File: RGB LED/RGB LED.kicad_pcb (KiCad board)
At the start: 2 copper layers, 80 x 75 mm, 81 parts, among them J1 USB_C_Receptacle_USB2.0_16P, SW1 SW_SPST, SW2 SW_SPST, U1 AP2112K-3.3, U2 MAX7219, U3 ESP32-S3-WROOM-1-N4

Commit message: schematic edits
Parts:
- added R4: 10K, Resistor_SMD:R_0603_1608Metric, F.Cu at (121.0, 82.9)
- C4: value 1uf 6.3V Y5V -> 1uF 6.3V Y5V
- D1, D2, D3, D4, D5, D6, D7, D8: value LED -> Green LED
- D10, D11, D12, D13, D14, D15, D16, D9: value LED -> Dark Blue LED
- D17, D19, D21, D23, D25, D27, D29, D31: value LED -> White LED
- D18, D20, D22, D24, D26, D28, D30, D32: value LED -> Purple LED
- D33, D37, D41, D45, D49, D53, D57, D61: value LED -> Red LED
- D34, D38, D42, D46, D50, D54, D58, D62: value LED -> Orange LED
- D35, D39, D43, D47, D51, D55, D59, D63: value LED -> Yellow LED
- D36, D40, D44, D48, D52, D56, D60, D64: value LED -> Light Blue LED
- R1: value 10k -> 5.1K 1%
- SW1, SW2: value SW_SPST -> SW_SPST_FSMSM
- TP1: value TestPoint -> RCWTE
- renumbered CIN1 to C5, COUT1 to C6
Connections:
- D65 pad 1: /ESP32/NEOPIXEL_PWR -> unconnected-(D65-DOUT-Pad1)
- D65 pad 3: unconnected-(D65-DIN-Pad3) -> /ESP32/NEOPIXEL
- D65 pad 4: /ESP32/NEOPIXEL -> /ESP32/NEOPIXEL_PWR
- U2 pad 18: unconnected-(U2-ISET-Pad18) -> Net-(U2-ISET)

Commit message: layout update
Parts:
- moved C6 70.3 mm to (75.8, 22.9)
- moved C5 70.3 mm to (75.8, 20.4)
- moved U1 70.3 mm to (80.4, 21.4)
- moved D14 59.2 mm to (96.3, 95.6)
- moved D15 59.2 mm to (96.3, 98.2)
- moved D19 59.2 mm to (96.3, 108.5)
- moved D20 59.2 mm to (96.3, 111.1)
- moved D25 59.2 mm to (100.4, 95.6)
- moved D26 59.2 mm to (100.4, 98.2)
- moved D3 59.2 mm to (92.3, 95.6)
- moved D30 59.2 mm to (100.4, 108.5)
- moved D36 59.2 mm to (104.4, 95.6)
- moved D37 59.2 mm to (104.4, 98.2)
- moved D4 59.2 mm to (92.3, 98.2)
- moved D41 59.2 mm to (104.4, 108.5)
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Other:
- board size 80 x 75 mm -> 119.2 x 110.4 mm

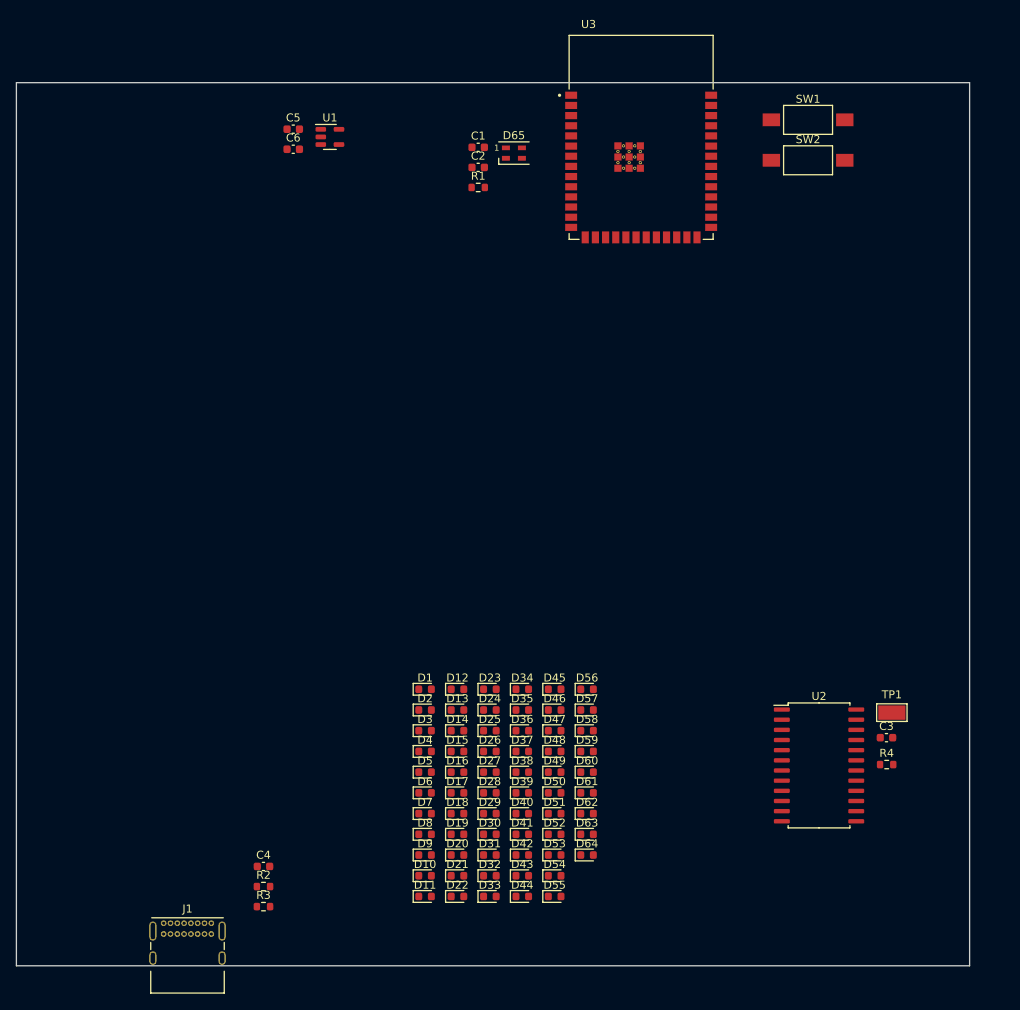
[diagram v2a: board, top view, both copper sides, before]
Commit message: changed layout, added traces/vias
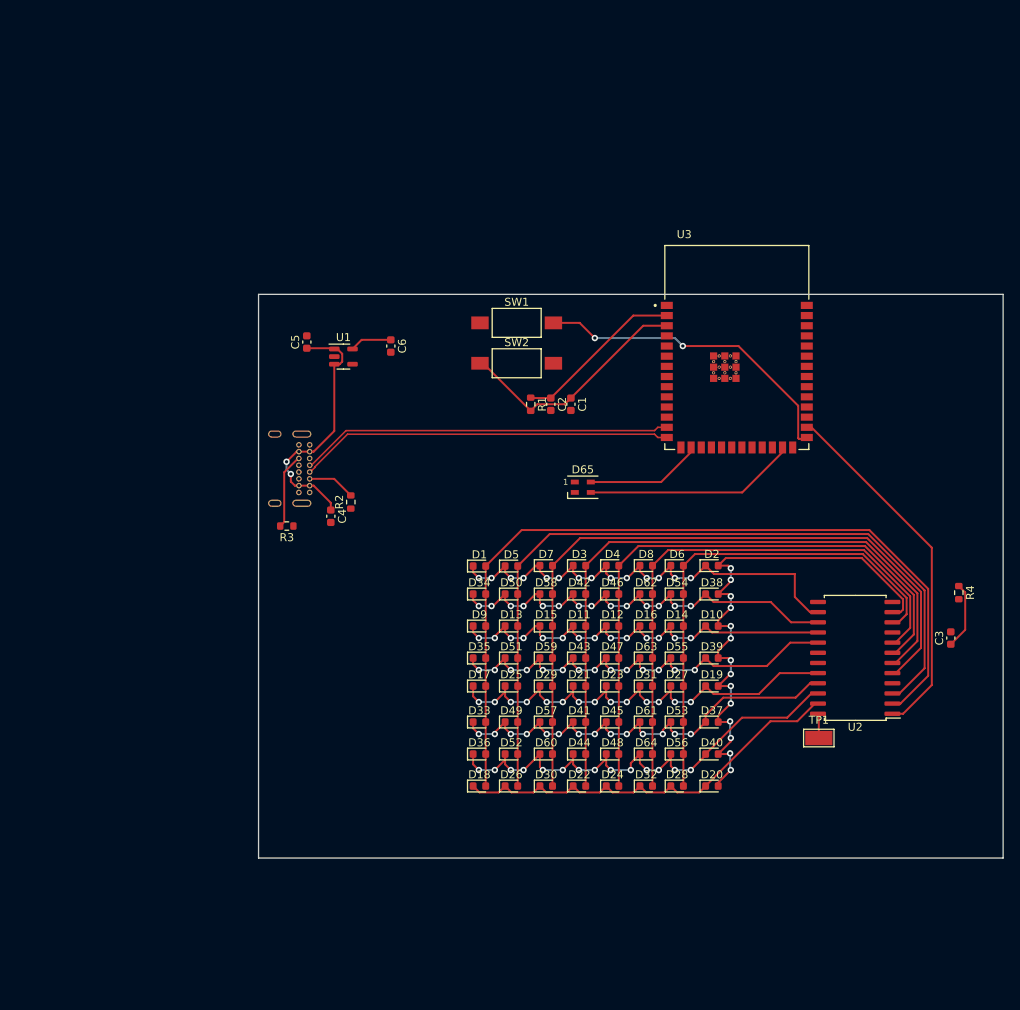
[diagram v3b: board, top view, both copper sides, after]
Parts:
- J1: moved to B.Cu
- moved J1 56.9 mm to (77.9, 65.8), turned to 90 degrees
- moved R2 49.3 mm to (83.0, 67.0), turned to 90 degrees
- moved R3 47.7 mm to (75.0, 70.0), turned to 180 degrees
- moved D10 47.5 mm to (128.1, 82.5)
- moved C4 44.6 mm to (80.5, 68.8), turned to -90 degrees
- moved SW1 44.4 mm to (103.7, 44.6)
- moved SW2 44.4 mm to (103.7, 49.7)
- moved D8 43.5 mm to (119.9, 75.0)
- moved D65 42.7 mm to (112.0, 65.2)
- moved D6 42.4 mm to (123.8, 75.0)
- moved D2 40.1 mm to (128.1, 75.0)
- moved D11 38.9 mm to (111.6, 82.5)
- moved D54 38.4 mm to (123.8, 78.5)
- moved D19 36.8 mm to (128.1, 90.0)
- moved D7 34.5 mm to (107.4, 75.0)
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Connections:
- D10 pad 2: /LED_Matrix/DIG_0 -> /LED_Matrix/DIG_1
- D11 pad 2: /LED_Matrix/DIG_0 -> /LED_Matrix/DIG_2
- D12 pad 2: /LED_Matrix/DIG_0 -> /LED_Matrix/DIG_3
- D13 pad 2: /LED_Matrix/DIG_0 -> /LED_Matrix/DIG_4
- D14 pad 2: /LED_Matrix/DIG_0 -> /LED_Matrix/DIG_5
- D15 pad 2: /LED_Matrix/DIG_0 -> /LED_Matrix/DIG_6
- D19 pad 2: /LED_Matrix/DIG_0 -> /LED_Matrix/DIG_1
- D2 pad 2: /LED_Matrix/DIG_0 -> /LED_Matrix/DIG_1
- D20 pad 2: /LED_Matrix/DIG_0 -> /LED_Matrix/DIG_1
- D21 pad 2: /LED_Matrix/DIG_0 -> /LED_Matrix/DIG_2
- D22 pad 2: /LED_Matrix/DIG_0 -> /LED_Matrix/DIG_2
- D23 pad 2: /LED_Matrix/DIG_0 -> /LED_Matrix/DIG_3
- D24 pad 2: /LED_Matrix/DIG_0 -> /LED_Matrix/DIG_3
- D25 pad 2: /LED_Matrix/DIG_0 -> /LED_Matrix/DIG_4
- D26 pad 2: /LED_Matrix/DIG_0 -> /LED_Matrix/DIG_4
- D27 pad 2: /LED_Matrix/DIG_0 -> /LED_Matrix/DIG_5
- D28 pad 2: /LED_Matrix/DIG_0 -> /LED_Matrix/DIG_5
- D29 pad 2: /LED_Matrix/DIG_0 -> /LED_Matrix/DIG_6
- D3 pad 2: /LED_Matrix/DIG_0 -> /LED_Matrix/DIG_2
- D30 pad 2: /LED_Matrix/DIG_0 -> /LED_Matrix/DIG_6
- D36 pad 1: /LED_Matrix/DIG_0 -> /LED_Matrix/SEG_DP
- D37 pad 2: /LED_Matrix/DIG_0 -> /LED_Matrix/DIG_1
- D38 pad 2: /LED_Matrix/DIG_0 -> /LED_Matrix/DIG_1
- D39 pad 2: /LED_Matrix/DIG_0 -> /LED_Matrix/DIG_1
- D4 pad 2: /LED_Matrix/DIG_0 -> /LED_Matrix/DIG_3
- D40 pad 1: /LED_Matrix/DIG_0 -> /LED_Matrix/SEG_DP
- D40 pad 2: /LED_Matrix/DIG_0 -> /LED_Matrix/DIG_1
- D41 pad 2: /LED_Matrix/DIG_0 -> /LED_Matrix/DIG_2
- D42 pad 2: /LED_Matrix/DIG_0 -> /LED_Matrix/DIG_2
- D43 pad 2: /LED_Matrix/DIG_0 -> /LED_Matrix/DIG_2
- D44 pad 1: /LED_Matrix/DIG_0 -> /LED_Matrix/SEG_DP
- D44 pad 2: /LED_Matrix/DIG_0 -> /LED_Matrix/DIG_2
- D45 pad 2: /LED_Matrix/DIG_0 -> /LED_Matrix/DIG_3
- D46 pad 2: /LED_Matrix/DIG_0 -> /LED_Matrix/DIG_3
- D47 pad 2: /LED_Matrix/DIG_0 -> /LED_Matrix/DIG_3
- D48 pad 1: /LED_Matrix/DIG_0 -> /LED_Matrix/SEG_DP
- D48 pad 2: /LED_Matrix/DIG_0 -> /LED_Matrix/DIG_3
- D49 pad 2: /LED_Matrix/DIG_0 -> /LED_Matrix/DIG_4
- D5 pad 2: /LED_Matrix/DIG_0 -> /LED_Matrix/DIG_4
- D50 pad 2: /LED_Matrix/DIG_0 -> /LED_Matrix/DIG_4
- D51 pad 2: /LED_Matrix/DIG_0 -> /LED_Matrix/DIG_4
- D52 pad 1: /LED_Matrix/DIG_0 -> /LED_Matrix/SEG_DP
- D52 pad 2: /LED_Matrix/DIG_0 -> /LED_Matrix/DIG_4
- D53 pad 2: /LED_Matrix/DIG_0 -> /LED_Matrix/DIG_5
- D54 pad 2: /LED_Matrix/DIG_0 -> /LED_Matrix/DIG_5
- D55 pad 2: /LED_Matrix/DIG_0 -> /LED_Matrix/DIG_5
- D56 pad 1: /LED_Matrix/DIG_0 -> /LED_Matrix/SEG_DP
- D56 pad 2: /LED_Matrix/DIG_0 -> /LED_Matrix/DIG_5
- D57 pad 2: /LED_Matrix/DIG_0 -> /LED_Matrix/DIG_6
- D58 pad 2: /LED_Matrix/DIG_0 -> /LED_Matrix/DIG_6
- D59 pad 2: /LED_Matrix/DIG_0 -> /LED_Matrix/DIG_6
- D6 pad 2: /LED_Matrix/DIG_0 -> /LED_Matrix/DIG_5
- D60 pad 1: /LED_Matrix/DIG_0 -> /LED_Matrix/SEG_DP
- D60 pad 2: /LED_Matrix/DIG_0 -> /LED_Matrix/DIG_6
- D64 pad 1: /LED_Matrix/DIG_0 -> /LED_Matrix/SEG_DP
- D7 pad 2: /LED_Matrix/DIG_0 -> /LED_Matrix/DIG_6
- U2 pad 10: /LED_Matrix/DIG_0 -> /LED_Matrix/DIG_5
- U2 pad 11: /LED_Matrix/DIG_0 -> /LED_Matrix/DIG_1
- U2 pad 22: /LED_Matrix/DIG_0 -> /LED_Matrix/SEG_DP
- U2 pad 3: /LED_Matrix/DIG_0 -> /LED_Matrix/DIG_4
- U2 pad 5: /LED_Matrix/DIG_0 -> /LED_Matrix/DIG_6
- U2 pad 6: /LED_Matrix/DIG_0 -> /LED_Matrix/DIG_2
- U2 pad 7: /LED_Matrix/DIG_0 -> /LED_Matrix/DIG_3
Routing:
- net /LED_Matrix/DIG_0: track 0.00 -> 104.5 mm
- net /LED_Matrix/DIG_4: track 0.00 -> 98.0 mm
- net /LED_Matrix/DIG_6: track 0.00 -> 89.7 mm
- net /LED_Matrix/DIG_2: track 0.00 -> 83.1 mm
- net /LED_Matrix/DIG_3: track 0.00 -> 76.5 mm
- net /LED_Matrix/DIG_1: track 0.00 -> 71.2 mm, vias 0 -> 14
- net /LED_Matrix/DIG_7: track 0.00 -> 69.9 mm
- net /LED_Matrix/SEG_DP: track 0.00 -> 65.5 mm, vias 0 -> 14
- net /LED_Matrix/SEG_C: track 0.00 -> 63.5 mm, vias 0 -> 14
- net /LED_Matrix/DIG_5: track 0.00 -> 62.6 mm
- net /LED_Matrix/SEG_A: track 0.00 -> 59.6 mm, vias 0 -> 14
- net /LED_Matrix/SEG_E: track 0.00 -> 58.3 mm, vias 0 -> 14
- net /LED_Matrix/SEG_G: track 0.00 -> 57.7 mm, vias 0 -> 14
- net /LED_Matrix/SEG_F: track 0.00 -> 56.8 mm, vias 0 -> 14
- net /LED_Matrix/SEG_B: track 0.00 -> 56.0 mm, vias 0 -> 14
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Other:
- board size 119.2 x 110.4 mm -> 93.1 x 70.5 mm

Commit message: draft of layout
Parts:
- added TP2: TestPoint, TestPoint:TestPoint_Keystone_5015_Micro-Minature, F.Cu at (76.5, 51.0)
- moved C3 24.8 mm to (133.5, 87.8)
- moved R4 23.1 mm to (137.0, 85.5)
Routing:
- net /~{CS}: track 0.00 -> 34.9 mm, vias 0 -> 2
- net /CLK: track 0.00 -> 32.7 mm, vias 0 -> 2
- net GND: track 0.00 -> 26.8 mm, vias 0 -> 16
- net +5V: track 8.35 -> 19.0 mm, vias 0 -> 2
- net Net-(U2-ISET): track 0.00 -> 4.60 mm
- net VBUS: track 32.4 -> 36.1 mm
- added copper zone on B.Cu, net GND
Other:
- board size 93.1 x 70.5 mm -> 93.1 x 66.5 mm
- board text added: "V_USB"

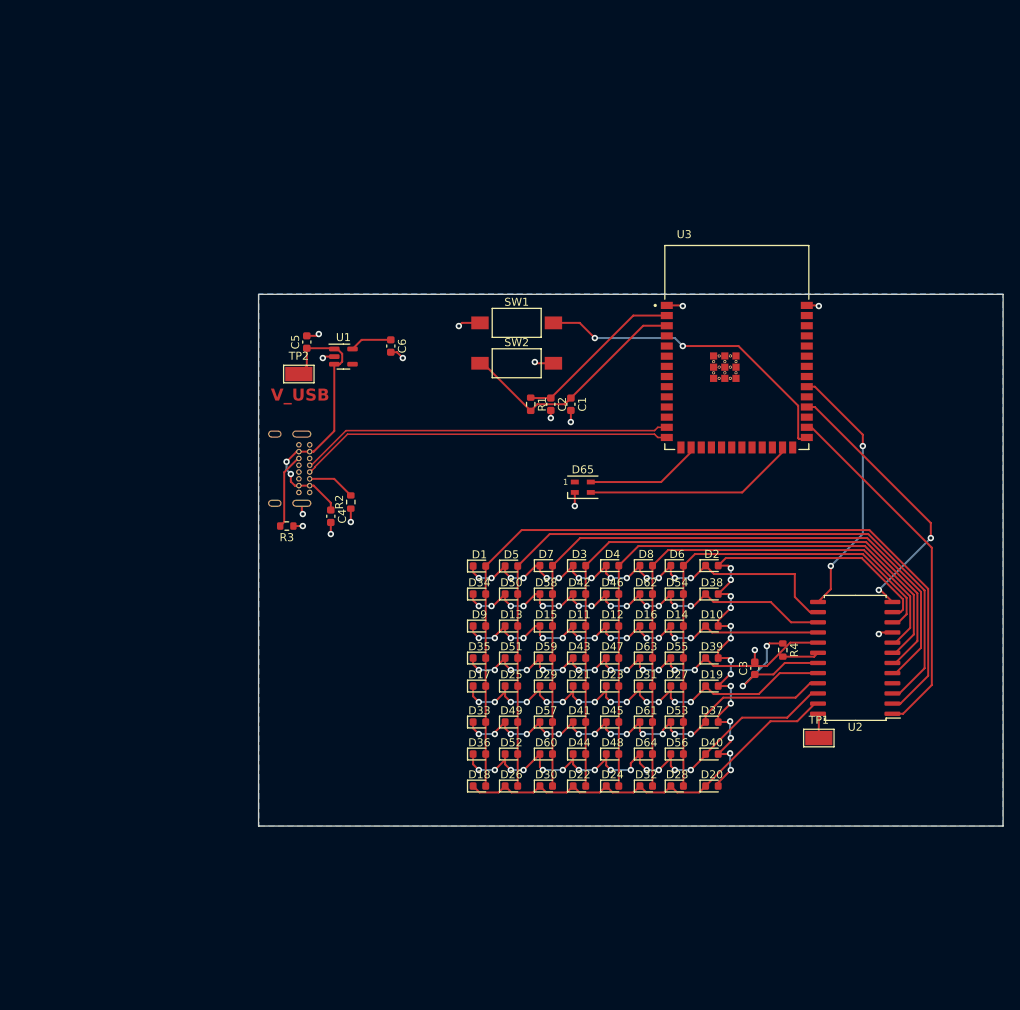
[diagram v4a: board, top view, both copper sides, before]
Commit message: edited layout according to feedback
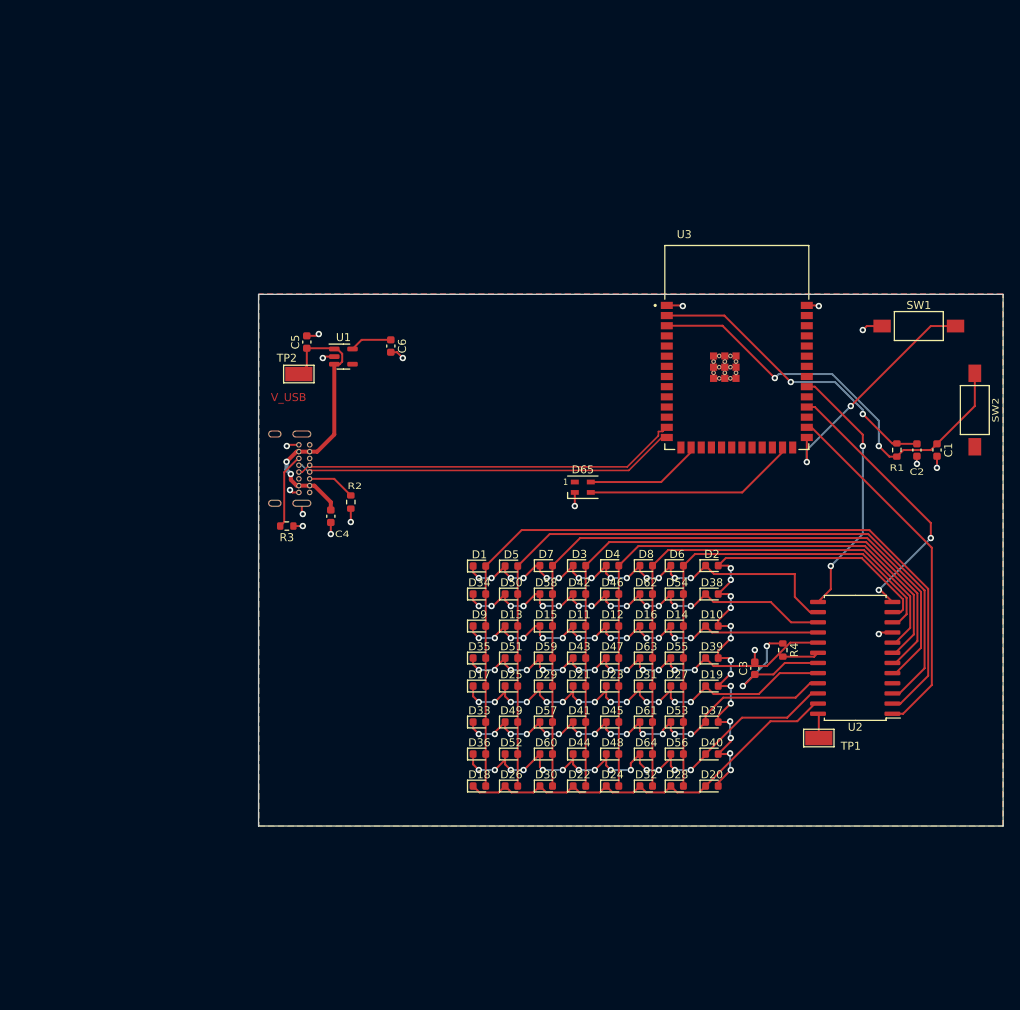
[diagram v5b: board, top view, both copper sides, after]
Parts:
- moved SW2 57.6 mm to (161.0, 55.5), turned to -90 degrees
- moved SW1 50.3 mm to (154.0, 45.0)
- moved C1 46.1 mm to (156.3, 60.5)
- moved R1 46.1 mm to (151.3, 60.5)
- moved C2 46.1 mm to (153.8, 60.5)
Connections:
- U3 pad 41_10: (no net) -> GND
- U3 pad 41_11: (no net) -> GND
- U3 pad 41_12: (no net) -> GND
- U3 pad 41_13: (no net) -> GND
- U3 pad 41_14: (no net) -> GND
- U3 pad 41_15: (no net) -> GND
- U3 pad 41_16: (no net) -> GND
- U3 pad 41_17: (no net) -> GND
- U3 pad 41_18: (no net) -> GND
- U3 pad 41_19: (no net) -> GND
- U3 pad 41_20: (no net) -> GND
- U3 pad 41_21: (no net) -> GND
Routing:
- net /ESP32/RESET: track 30.2 -> 54.3 mm, vias 0 -> 2
- net +3.3V: track 21.3 -> 38.2 mm, vias 0 -> 2
- net /ESP32/BOOT: track 40.1 -> 29.8 mm
- net /USB_N: track 46.6 -> 49.0 mm
- net /USB_P: track 46.8 -> 48.4 mm
- net GND: track 26.8 -> 27.0 mm, vias 16 -> 17
- added copper zone on F.Cu, net GND

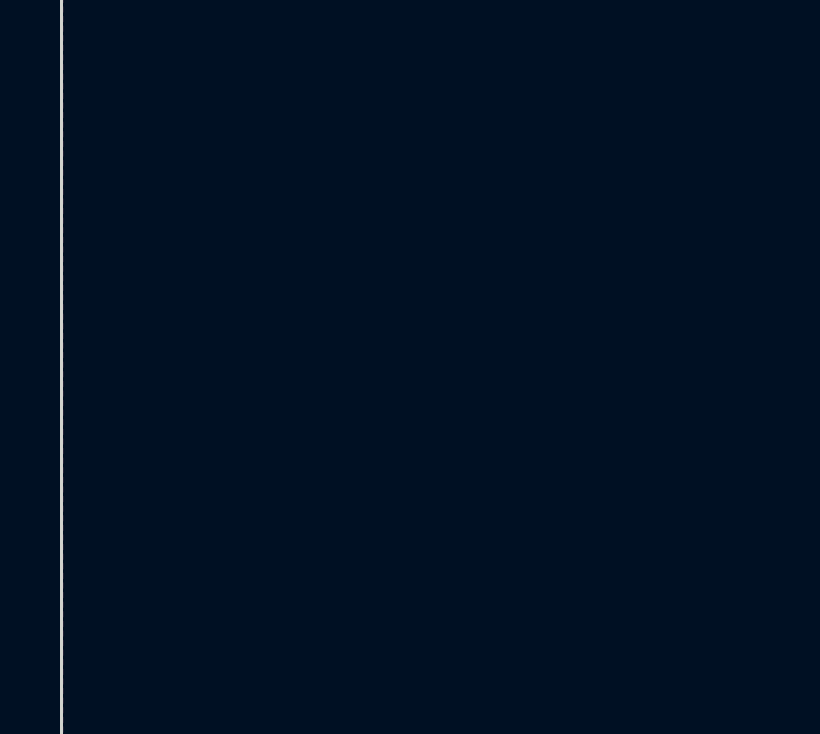
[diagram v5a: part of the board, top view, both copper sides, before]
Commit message: added logos
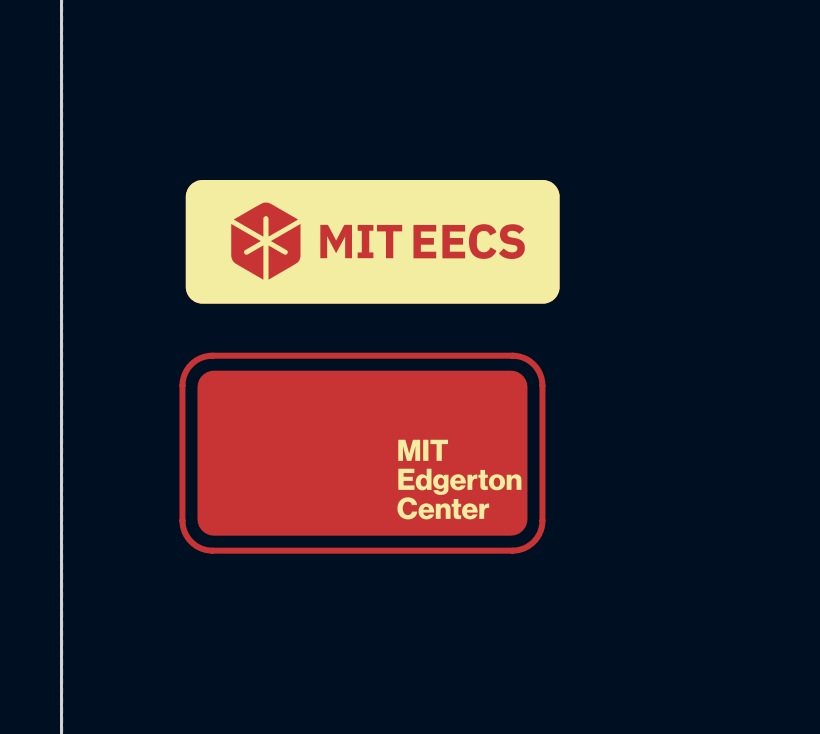
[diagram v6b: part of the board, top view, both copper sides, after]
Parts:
- added REF**: EdgertonLogo, Graphics:EdgertonLogo, F.Cu at (76.0, 84.5)
- added REF**: EECSLogo, Graphics:EECSLogo, F.Cu at (75.5, 78.0)

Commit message: added meche logo
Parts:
- added REF**: MechELogo, Graphics:MechELogo, F.Cu at (76.0, 92.5)
